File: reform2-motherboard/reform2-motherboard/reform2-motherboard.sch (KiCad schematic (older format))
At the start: 45 parts, among them J15 Conn_01x33, J18 Conn_01x03_Male, J19 JTAG, J20 Conn_01x03_Male, SW3 SW_DIP_x01, SW6 SW_Push, U1 Nitrogen8M

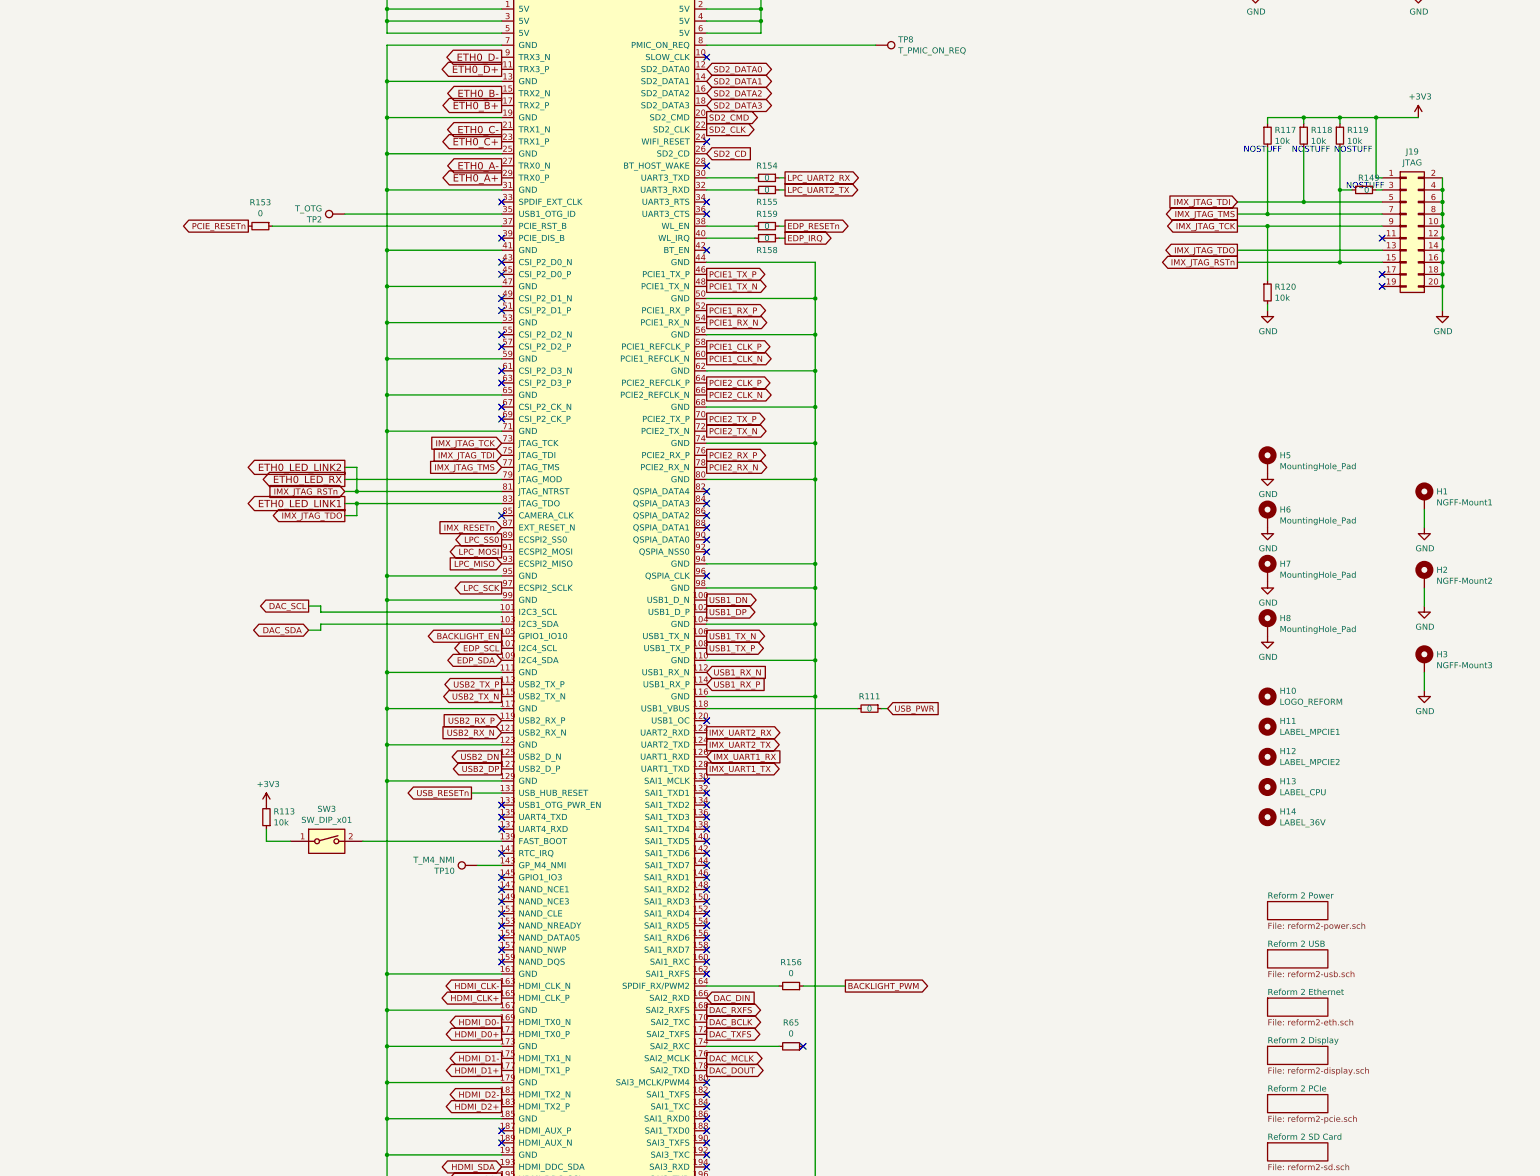
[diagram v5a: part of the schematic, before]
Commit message: Reform 2 Rev 2 WIP: fixed various Rev 1 bugs; consolidate battery connector; consolidate 5v powers; make power rails switchable by LPC; exchange TUSB QFN for TQFP; remove eDP FPC; fixes holes; add SD level shifter; add PCIe clock generator; reduce JTAG footprint
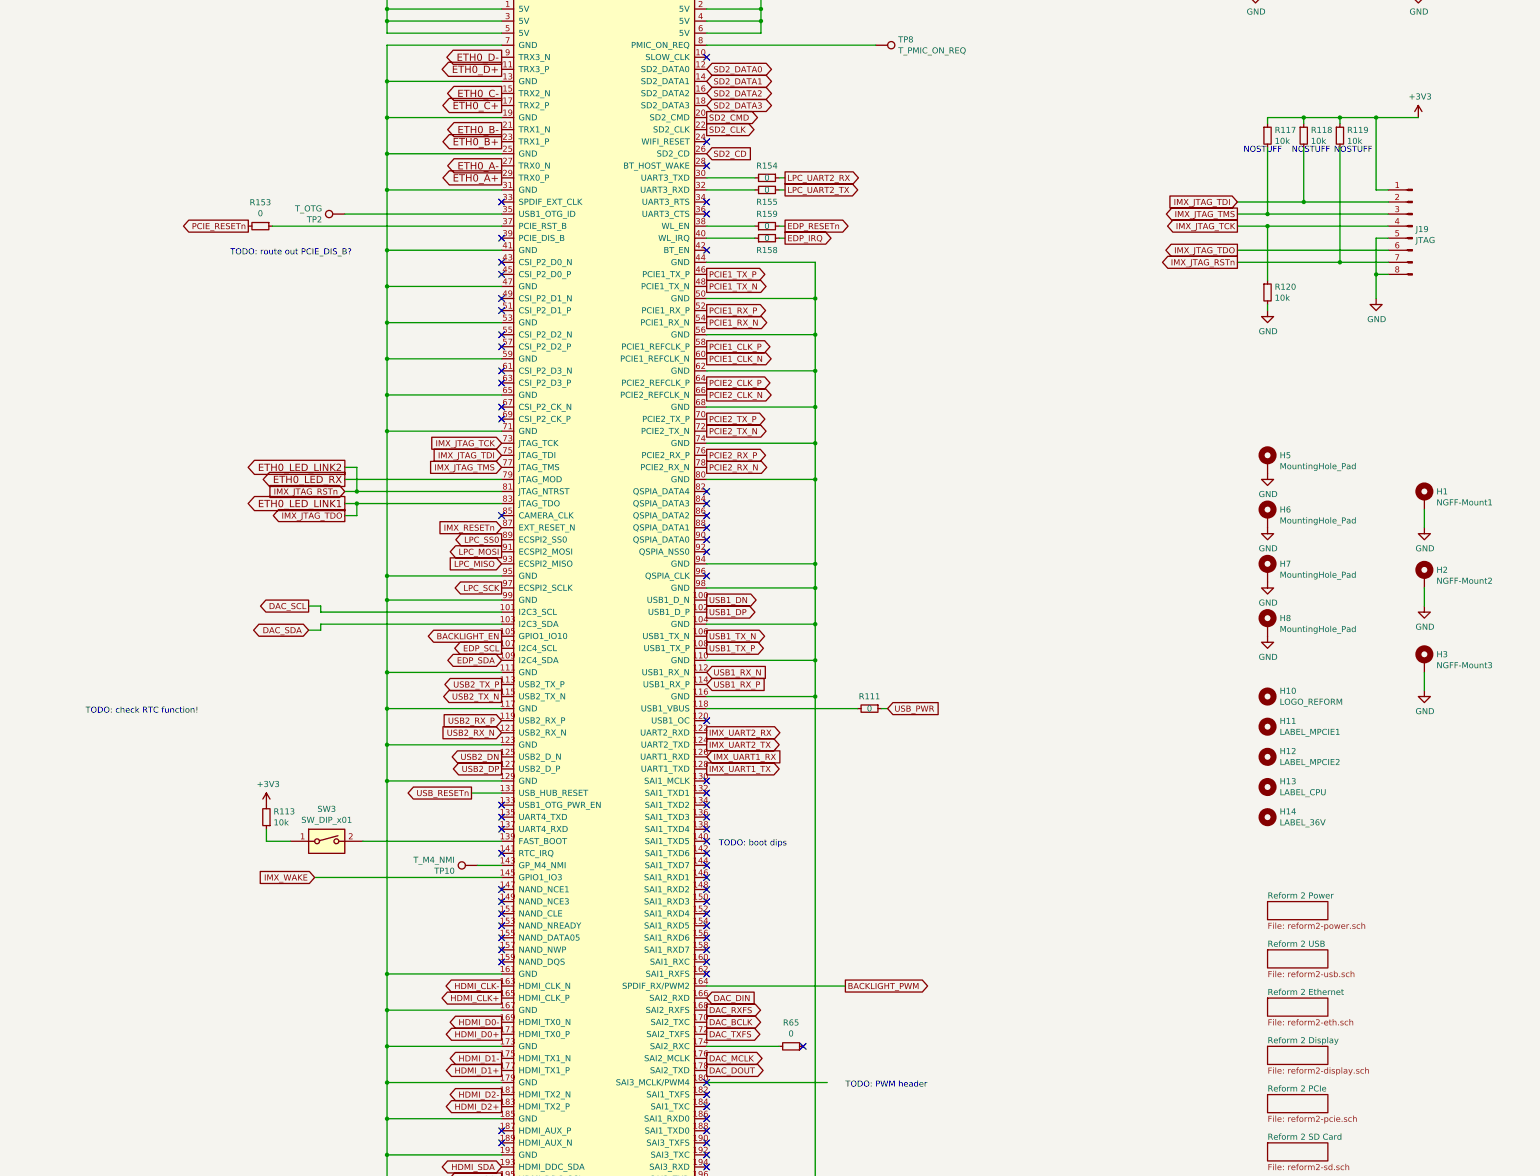
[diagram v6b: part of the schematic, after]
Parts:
- removed J19: JTAG, Connector_PinHeader_2.54mm:PinHeader_2x10_P2.54mm_Vertical, symbol Connector_Generic:Conn_02x10_Odd_Even
- removed R149, R156: 0, Resistor_SMD:R_0603_1608Metric, symbol Device:R_Small
- added J19: JTAG, Connector_PinHeader_2.54mm:PinHeader_2x04_P2.54mm_Vertical, symbol Connector:Conn_01x08_Male
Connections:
- net +3V3: now also J19.1 (Pin_1)
- net BACKLIGHT_PWM: now also U1.164 (SPDIF_RX/PWM2)
- net ETH0_B+: now also U1.23 (TRX1_P); no longer U1.17 (TRX2_P)
- net ETH0_B-: now also U1.21 (TRX1_N); no longer U1.15 (TRX2_N)
- net ETH0_C+: now also U1.17 (TRX2_P); no longer U1.23 (TRX1_P)
- net ETH0_C-: now also U1.15 (TRX2_N); no longer U1.21 (TRX1_N)
- net ETH0_LED_LINK1: now also J19.6 (Pin_6)
- net ETH0_LED_LINK2: now also J19.7 (Pin_7)
- net GND: now also J19.5 (Pin_5), J19.8 (Pin_8)
- net IMX_JTAG_TCK: now also J19.4 (Pin_4)
- net IMX_JTAG_TDI: now also J19.2 (Pin_2)
- net IMX_JTAG_TMS: now also J19.3 (Pin_3)
- net IMX_WAKE: now reaches U1.145 (GPIO1_IO3)
- no-connect marks 87 -> 83
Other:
- note added: "TODO: PWM header"
- note added: "TODO: boot dips"
- note added: "TODO: check RTC function!"
- note added: "TODO: route out PCIE_DIS_B?"
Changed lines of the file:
@@
 Sheet 1 9
 Title "MNT Reform 2"
-Date "2019-07-18"
-Rev "2.0D-1"
+Date "2019-09-24"
+Rev "2.0D-2"
 Comp "MNT Research GmbH"
 Comment1 "https://mntre.com"
@@
 Text GLabel 8700 7950 0    50   Output ~ 0
 LPC_SS0
-Wire Wire Line
-	11000 11650 10400 11650
-Wire Wire Line
-	11200 11650 11550 11650
-$Comp
-L Device:R_Small R156
-U 1 1 61B3EC18
-P 11100 11650
-F 0 "R156" V 11296 11650 50  0000 C CNN
-F 1 "0" V 11205 11650 50  0000 C CNN
-F 2 "Resistor_SMD:R_0603_1608Metric" H 11100 11650 50  0001 C CNN
-F 3 "~" H 11100 11650 50  0001 C CNN
-F 4 "Vishay Dale" H 11100 11650 50  0001 C CNN "Manufacturer"
-F 5 "CRCW06030000Z0EAC" H 11100 11650 50  0001 C CNN "Manufacturer_No"
-	1    11100 11650
-	0    1    -1   0
-$EndComp
 NoConn ~ 10400 9450
 Text GLabel 6600 5350 0    50   Output ~ 0
@@
 Text GLabel 8450 10050 0    50   Output ~ 0
 USB_RESETn
-NoConn ~ 8700 10750
 NoConn ~ 8700 10550
 $Comp
@@
 	1    0    0    -1
 $EndComp
-Text Notes 15700 5050 0    50   ~ 0
-NOSTUFF
-Wire Wire Line
-	15650 5050 15650 5650
-Connection ~ 15650 5050
-Wire Wire Line
-	15750 5050 15650 5050
-Wire Wire Line
-	15950 5050 16000 5050
-$Comp
-L Device:R_Small R149
-U 1 1 5F15012C
-P 15850 5050
-F 0 "R149" V 15750 5000 50  0000 L CNN
-F 1 "0" V 15850 5050 50  0000 L CNN
-F 2 "Resistor_SMD:R_0603_1608Metric" H 15850 5050 50  0001 C CNN
-F 3 "~" H 15850 5050 50  0001 C CNN
-F 4 "Vishay Dale" H 15850 5050 50  0001 C CNN "Manufacturer"
-F 5 "CRCW06030000Z0EAC" H 15850 5050 50  0001 C CNN "Manufacturer_No"
-	1    15850 5050
-	0    1    1    0
-$EndComp
 Connection ~ 15650 5650
 Wire Wire Line
 	15650 5650 14800 5650
 Wire Wire Line
-	15650 4700 15650 5050
-Wire Wire Line
-	15650 5650 16000 5650
-Connection ~ 16500 5850
-Wire Wire Line
-	16500 6050 16500 5850
-Wire Wire Line
-	16500 5750 16500 5850
-Connection ~ 16500 5750
-Wire Wire Line
-	16500 5650 16500 5750
-Connection ~ 16500 5650
-Wire Wire Line
-	16500 5550 16500 5650
-Connection ~ 16500 5550
-Wire Wire Line
-	16500 5450 16500 5550
-Connection ~ 16500 5450
-Wire Wire Line
-	16500 5350 16500 5450
-Connection ~ 16500 5350
-Wire Wire Line
-	16500 5250 16500 5350
-Connection ~ 16500 5250
-Wire Wire Line
-	16500 5150 16500 5250
-Connection ~ 16500 5150
-Wire Wire Line
-	16500 5050 16500 5150
-Connection ~ 16500 5050
-Wire Wire Line
-	16500 4950 16500 5050
+	15650 5650 16050 5650
+Wire Wire Line
+	15950 5950 15950 5750
 $Comp
 L power:GND #PWR0219
 U 1 1 5F0CE58E
-P 16500 6050
-F 0 "#PWR0219" H 16500 5800 50  0001 C CNN
-F 1 "GND" H 16505 5877 50  0000 C CNN
-F 2 "" H 16500 6050 50  0001 C CNN
-F 3 "" H 16500 6050 50  0001 C CNN
-	1    16500 6050
+P 15950 5950
+F 0 "#PWR0219" H 15950 5700 50  0001 C CNN
+F 1 "GND" H 15955 5777 50  0000 C CNN
+F 2 "" H 15950 5950 50  0001 C CNN
+F 3 "" H 15950 5950 50  0001 C CNN
+	1    15950 5950
 	1    0    0    -1
 $EndComp
@@
 	15950 4450 15650 4450
 Connection ~ 15950 4450
-Wire Wire Line
-	15950 4950 16000 4950
-Wire Wire Line
-	15950 4450 15950 4950
 Wire Wire Line
 	15050 6050 15050 6000
@@
 	1    0    0    -1
 $EndComp
-NoConn ~ 16000 5850
-NoConn ~ 16000 5750
-NoConn ~ 16000 5450
-Wire Wire Line
-	16000 5550 14800 5550
-Wire Wire Line
-	15050 5350 16000 5350
+Wire Wire Line
+	16050 5550 14800 5550
+Wire Wire Line
+	15050 5350 16050 5350
 Connection ~ 15050 5350
 Wire Wire Line
@@
 Connection ~ 15050 5250
 Wire Wire Line
-	15050 5250 16000 5250
+	15050 5250 16050 5250
 Wire Wire Line
 	15050 5250 14800 5250
@@
 Connection ~ 15350 5150
 Wire Wire Line
-	15350 5150 16000 5150
+	15350 5150 16050 5150
 Wire Wire Line
 	15350 5150 14800 5150
@@
 Text GLabel 14800 5250 0    50   Output ~ 0
 IMX_JTAG_TMS
-$Comp
-L Connector_Generic:Conn_02x10_Odd_Even J19
-U 1 1 5EEB8075
-P 16200 5350
-F 0 "J19" H 16250 5967 50  0000 C CNN
-F 1 "JTAG" H 16250 5876 50  0000 C CNN
-F 2 "Connector_PinHeader_2.54mm:PinHeader_2x10_P2.54mm_Vertical" H 16200 5350 50  0001 C CNN
-F 3 "~" H 16200 5350 50  0001 C CNN
-F 4 "Molex" H 16200 5350 50  0001 C CNN "Manufacturer"
-F 5 "87914-2016" H 16200 5350 50  0001 C CNN "Manufacturer_No"
-	1    16200 5350
-	1    0    0    -1
-$EndComp
 $Comp
 L power:+4V #PWR025
@@
 Text GLabel 8700 4850 0    60   Output ~ 0
 ETH0_A-
+Text GLabel 8700 4650 0    60   Output ~ 0
+ETH0_B+
+Text GLabel 8700 4550 0    60   Output ~ 0
+ETH0_B-
 Text GLabel 8700 4350 0    60   Output ~ 0
-ETH0_B+
+ETH0_C+
 Text GLabel 8700 4250 0    60   Output ~ 0
-ETH0_B-
-Text GLabel 8700 4650 0    60   Output ~ 0
-ETH0_C+
-Text GLabel 8700 4550 0    60   Output ~ 0
 ETH0_C-
 Text GLabel 8700 4050 0    60   Output ~ 0
@@
 Wire Wire Line
 	8700 10650 8500 10650
+Wire Wire Line
+	10400 11650 11550 11650
+Text Notes 6450 5600 0    50   ~ 0
+TODO: route out PCIE_DIS_B?
+Wire Wire Line
+	10400 12450 11400 12450
+Text Notes 11550 12500 0    50   ~ 0
+TODO: PWM header
+Text Notes 10500 10500 0    50   ~ 0
+TODO: boot dips
+Text Notes 5250 9400 0    50   ~ 0
+TODO: check RTC function!
+Wire Wire Line
+	8700 10750 7150 10750
+Text GLabel 7150 10750 0    50   Input ~ 0
+IMX_WAKE
+Wire Wire Line
+	15650 4700 15650 5650
+$Comp
+L Connector:Conn_01x08_Male J19
+U 1 1 5ECAAFCE
+P 16250 5350
+F 0 "J19" H 16222 5324 50  0000 R CNN
+F 1 "JTAG" H 16222 5233 50  0000 R CNN
+F 2 "Connector_PinHeader_2.54mm:PinHeader_2x04_P2.54mm_Vertical" H 16250 5350 50  0001 C CNN
+F 3 "~" H 16250 5350 50  0001 C CNN
+	1    16250 5350
+	-1   0    0    -1
+$EndComp
+Wire Wire Line
+	16050 5750 15950 5750
+Wire Wire Line
+	16050 5050 15950 5050
+Wire Wire Line
+	15950 4450 15950 5050
+Wire Wire Line
+	15950 5750 15950 5450
+Wire Wire Line
+	15950 5450 16050 5450
+Connection ~ 15950 5750
 $EndSCHEMATC

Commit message: reform2 motherboard: finalize BOM
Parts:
- J19: Manufacturer (none) -> Wurth; Manufacturer_No (none) -> 87914-0816
- SW6: Manufacturer_No KMR2 -> KMR223NGULCLFG
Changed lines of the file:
@@
 F 3 "~" H 15350 2100 50  0001 C CNN
 F 4 "CK" H 15350 1900 50  0001 C CNN "Manufacturer"
-F 5 "KMR2" H 15350 1900 50  0001 C CNN "Manufacturer_No"
+F 5 "KMR223NGULCLFG" H 15350 1900 50  0001 C CNN "Manufacturer_No"
 	1    15350 1900
 	1    0    0    -1
@@
 F 2 "Connector_PinHeader_2.54mm:PinHeader_2x04_P2.54mm_Vertical" H 16250 5350 50  0001 C CNN
 F 3 "~" H 16250 5350 50  0001 C CNN
+F 4 "Wurth" H 16250 5350 50  0001 C CNN "Manufacturer"
+F 5 "87914-0816" H 16250 5350 50  0001 C CNN "Manufacturer_No"
 	1    16250 5350
 	-1   0    0    -1

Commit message: WIP reform2 motherboard routing almost complete
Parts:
- J19: Manufacturer Wurth -> Amphenol FCI; Manufacturer_No 87914-0816 -> 79425-408HLF
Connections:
- net +4V renamed +5V
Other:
- note added: "This is a i.MX8M internal oscillator output for PCIe1"
- note added: "This is refclk input (PAD_CLK) for PCIe2"
- note removed: "ACTUALLY 5V"
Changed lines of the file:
@@
 Wire Wire Line
 	8700 3550 7750 3550
-$Comp
-L power:+4V #PWR0104
-U 1 1 606EC9C2
-P 7750 2900
-F 0 "#PWR0104" H 7750 2750 50  0001 C CNN
-F 1 "+4V" H 7765 3073 50  0000 C CNN
-F 2 "" H 7750 2900 50  0001 C CNN
-F 3 "" H 7750 2900 50  0001 C CNN
-	1    7750 2900
-	-1   0    0    -1
-$EndComp
-Text Notes 8050 2600 2    50   ~ 0
-ACTUALLY 5V
 Wire Wire Line
 	7750 2900 7750 3550
@@
 Text GLabel 14800 5250 0    50   Output ~ 0
 IMX_JTAG_TMS
-$Comp
-L power:+4V #PWR025
-U 1 1 5E9AB42D
-P 10850 2900
-F 0 "#PWR025" H 10850 2750 50  0001 C CNN
-F 1 "+4V" H 10865 3073 50  0000 C CNN
-F 2 "" H 10850 2900 50  0001 C CNN
-F 3 "" H 10850 2900 50  0001 C CNN
-	1    10850 2900
-	1    0    0    -1
-$EndComp
-Text Notes 10550 2600 0    50   ~ 0
-ACTUALLY 5V
 Text GLabel 8700 8350 0    50   Output ~ 0
 LPC_SCK
@@
 Text GLabel 10400 6350 2    50   Output ~ 0
 PCIE1_CLK_P
-Text GLabel 10400 6750 2    50   Output ~ 0
+Text GLabel 10400 6750 2    50   Input ~ 0
 PCIE2_CLK_N
-Text GLabel 10400 6650 2    50   Output ~ 0
+Text GLabel 10400 6650 2    50   Input ~ 0
 PCIE2_CLK_P
 Text GLabel 10400 7250 2    50   Output ~ 0
@@
 F 2 "Connector_PinHeader_2.54mm:PinHeader_2x04_P2.54mm_Vertical" H 16250 5350 50  0001 C CNN
 F 3 "~" H 16250 5350 50  0001 C CNN
-F 4 "Wurth" H 16250 5350 50  0001 C CNN "Manufacturer"
-F 5 "87914-0816" H 16250 5350 50  0001 C CNN "Manufacturer_No"
+F 4 "Amphenol FCI" H 16250 5350 50  0001 C CNN "Manufacturer"
+F 5 "79425-408HLF" H 16250 5350 50  0001 C CNN "Manufacturer_No"
 	1    16250 5350
 	-1   0    0    -1
@@
 	15950 5450 16050 5450
 Connection ~ 15950 5750
+$Comp
+L power:+5V #PWR0104
+U 1 1 5EB50931
+P 7750 2900
+F 0 "#PWR0104" H 7750 2750 50  0001 C CNN
+F 1 "+5V" H 7765 3073 50  0000 C CNN
+F 2 "" H 7750 2900 50  0001 C CNN
+F 3 "" H 7750 2900 50  0001 C CNN
+	1    7750 2900
+	1    0    0    -1
+$EndComp
+$Comp
+L power:+5V #PWR0242
+U 1 1 5EB50E6D
+P 10850 2900
+F 0 "#PWR0242" H 10850 2750 50  0001 C CNN
+F 1 "+5V" H 10865 3073 50  0000 C CNN
+F 2 "" H 10850 2900 50  0001 C CNN
+F 3 "" H 10850 2900 50  0001 C CNN
+	1    10850 2900
+	1    0    0    -1
+$EndComp
+Text Notes 11000 6750 0    50   ~ 0
+This is refclk input (PAD_CLK) for PCIe2
+Text Notes 11000 6450 0    50   ~ 0
+This is a i.MX8M internal oscillator output for PCIe1
 $EndSCHEMATC
